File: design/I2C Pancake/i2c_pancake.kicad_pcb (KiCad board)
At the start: 4 copper layers, 74.9 x 45 mm, 41 parts, among them J1 Conn_01x03, J2 Conn_01x03, J3 Conn_01x05_Male, J4 Conn_01x04, J5 Conn_01x04, J6 Conn_01x04, J7 Conn_01x05_Male, J8 Conn_01x05_Female, SW1 SW_DIP_x04, U1 INA826, U2 TL750M10CKVU, U3 INA826, U4 INA826, U6 PIC16F1826-ISO

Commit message: Add test points to the Pancake board.
Test points were added to the outputs of each strain guage amp.
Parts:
- added STR1: TestPoint, custom:TestPoint, F.Cu at (128.1, 107.9)
- added STR2: TestPoint, custom:TestPoint, B.Cu at (135.6, 124.0)
- added STR3: TestPoint, custom:TestPoint, B.Cu at (115.6, 122.6)
- C3: footprint Capacitor_SMD:C_0805_2012Metric_Pad1.15x1.40mm_HandSolder -> footprints:C_0805_HandSoldering
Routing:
- net /STRAIN_OUT_2: track 36.8 -> 40.6 mm
- net /STRAIN_OUT_1: track 34.9 -> 37.9 mm
- net /STRAIN_OUT_3: track 24.4 -> 27.2 mm
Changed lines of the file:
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@@
     (thickness 1.6)
     (drawings 40)
-    (tracks 466)
+    (tracks 479)
     (zones 0)
-    (modules 41)
+    (modules 44)
     (nets 38)
   )
@@
     (mod_text_size 1 1)
     (mod_text_width 0.15)
-    (pad_size 6.7564 6.9342)
-    (pad_drill 0)
+    (pad_size 1.524 1.524)
+    (pad_drill 0.762)
     (pad_to_mask_clearance 0)
     (aux_axis_origin 0 0)
@@
     (add_net /SDA)
   )
+  (module custom:TestPoint (layer B.Cu)
+    (at 135.6026 124.0168)
+    (fp_text reference STR2 (at 0 -0.5) (layer B.SilkS)
+      (effects (font (size 1 1) (thickness 0.15)) (justify mirror))
+    )
+    (fp_text value TestPoint (at 0 0.5) (layer B.Fab)
+      (effects (font (size 1 1) (thickness 0.15)) (justify mirror))
+    )
+    (fp_circle (center 0 -3) (end 1 -3) (layer B.SilkS) (width 0.12))
+    (pad 1 thru_hole circle (at 0 -3) (size 1.524 1.524) (drill 0.762) (layers *.Cu *.Mask)
+      (net 6 /STRAIN_OUT_2))
+  )
+  (module custom:TestPoint (layer F.Cu)
+    (at 128.135 107.9386)
+    (fp_text reference STR1 (at 0 0.5) (layer F.SilkS)
+      (effects (font (size 1 1) (thickness 0.15)))
+    )
+    (fp_text value TestPoint (at 0 -0.5) (layer F.Fab)
+      (effects (font (size 1 1) (thickness 0.15)))
+    )
+    (fp_circle (center 0 3) (end 1 3) (layer F.SilkS) (width 0.12))
+    (pad 1 thru_hole circle (at 0 3) (size 1.524 1.524) (drill 0.762) (layers *.Cu *.Mask)
+      (net 7 /STRAIN_OUT_1))
+  )
+  (module footprints:C_0805_HandSoldering (layer B.Cu)
+    (at 149.09 107.8424 270)
+    (descr "Capacitor SMD 0805, hand soldering")
+    (tags "capacitor 0805")
+    (attr smd)
+    (fp_text reference C3 (at 3.302 0 90) (layer B.SilkS)
+      (effects (font (size 1 1) (thickness 0.15)) (justify mirror))
+    )
+    (fp_text value "10 uF" (at 0 -1.75 90) (layer B.Fab)
+      (effects (font (size 1 1) (thickness 0.15)) (justify mirror))
+    )
+    (fp_line (start 2.25 -0.87) (end -2.25 -0.87) (layer B.CrtYd) (width 0.05))
+    (fp_line (start 2.25 -0.87) (end 2.25 0.88) (layer B.CrtYd) (width 0.05))
+    (fp_line (start -2.25 0.88) (end -2.25 -0.87) (layer B.CrtYd) (width 0.05))
+    (fp_line (start -2.25 0.88) (end 2.25 0.88) (layer B.CrtYd) (width 0.05))
+    (fp_line (start -0.5 -0.85) (end 0.5 -0.85) (layer B.SilkS) (width 0.12))
+    (fp_line (start 0.5 0.85) (end -0.5 0.85) (layer B.SilkS) (width 0.12))
+    (fp_line (start -1 0.62) (end 1 0.62) (layer B.Fab) (width 0.1))
+    (fp_line (start 1 0.62) (end 1 -0.62) (layer B.Fab) (width 0.1))
+    (fp_line (start 1 -0.62) (end -1 -0.62) (layer B.Fab) (width 0.1))
+    (fp_line (start -1 -0.62) (end -1 0.62) (layer B.Fab) (width 0.1))
+    (fp_text user %R (at 0 1.75 90) (layer B.Fab)
+      (effects (font (size 1 1) (thickness 0.15)) (justify mirror))
+    )
+    (pad 2 smd rect (at 1.25 0 270) (size 1.5 1.25) (layers B.Cu B.Paste B.Mask)
+      (net 1 GND))
+    (pad 1 smd rect (at -1.25 0 270) (size 1.5 1.25) (layers B.Cu B.Paste B.Mask)
+      (net 2 +10V))
+    (model Capacitors_SMD.3dshapes/C_0805.wrl
+      (at (xyz 0 0 0))
+      (scale (xyz 1 1 1))
+      (rotate (xyz 0 0 0))
+    )
+  )
+  (module custom:TestPoint (layer B.Cu)
+    (at 115.6382 122.6198)
+    (fp_text reference STR3 (at 3.4798 -2.1844) (layer B.SilkS)
+      (effects (font (size 1 1) (thickness 0.15)) (justify mirror))
+    )
+    (fp_text value TestPoint (at 3.7846 -1.5748) (layer B.Fab)
+      (effects (font (size 1 1) (thickness 0.15)) (justify mirror))
+    )
+    (fp_circle (center 0 -3) (end 1 -3) (layer B.SilkS) (width 0.12))
+    (pad 1 thru_hole circle (at 0 -3) (size 1.524 1.524) (drill 0.762) (layers *.Cu *.Mask)
+      (net 5 /STRAIN_OUT_3))
+  )
   (module Fuse:Fuse_0805_2012Metric_Pad1.15x1.40mm_HandSolder (layer F.Cu)
     (at 142.994 113.2218 270)
@@
       (net 20 "Net-(C1-Pad1)"))
     (model ${KISYS3DMOD}/Fuse.3dshapes/Fuse_0805_2012Metric.wrl
-      (at (xyz 0 0 0))
-      (scale (xyz 1 1 1))
-      (rotate (xyz 0 0 0))
-    )
-  )
-  (module Capacitor_SMD:C_0805_2012Metric_Pad1.15x1.40mm_HandSolder (layer B.Cu)
-    (at 149.09 107.8424 270)
-    (descr "Capacitor SMD 0805 (2012 Metric), square (rectangular) end terminal, IPC_7351 nominal with elongated pad for handsoldering. (Body size source: https://docs.google.com/spreadsheets/d/1BsfQQcO9C6DZCsRaXUlFlo91Tg2WpOkGARC1WS5S8t0/edit?usp=sharing), generated with kicad-footprint-generator")
-    (tags "capacitor handsolder")
-    (attr smd)
-    (fp_text reference C3 (at 0 1.65 90) (layer B.SilkS)
-      (effects (font (size 1 1) (thickness 0.15)) (justify mirror))
-    )
-    (fp_text value "10 uF" (at 0 -1.65 90) (layer B.Fab)
-      (effects (font (size 1 1) (thickness 0.15)) (justify mirror))
-    )
-    (fp_text user %R (at 0 0 90) (layer B.Fab)
-      (effects (font (size 0.5 0.5) (thickness 0.08)) (justify mirror))
-    )
-    (fp_line (start 1.85 -0.95) (end -1.85 -0.95) (layer B.CrtYd) (width 0.05))
-    (fp_line (start 1.85 0.95) (end 1.85 -0.95) (layer B.CrtYd) (width 0.05))
-    (fp_line (start -1.85 0.95) (end 1.85 0.95) (layer B.CrtYd) (width 0.05))
-    (fp_line (start -1.85 -0.95) (end -1.85 0.95) (layer B.CrtYd) (width 0.05))
-    (fp_line (start -0.261252 -0.71) (end 0.261252 -0.71) (layer B.SilkS) (width 0.12))
-    (fp_line (start -0.261252 0.71) (end 0.261252 0.71) (layer B.SilkS) (width 0.12))
-    (fp_line (start 1 -0.6) (end -1 -0.6) (layer B.Fab) (width 0.1))
-    (fp_line (start 1 0.6) (end 1 -0.6) (layer B.Fab) (width 0.1))
-    (fp_line (start -1 0.6) (end 1 0.6) (layer B.Fab) (width 0.1))
-    (fp_line (start -1 -0.6) (end -1 0.6) (layer B.Fab) (width 0.1))
-    (pad 2 smd roundrect (at 1.025 0 270) (size 1.15 1.4) (layers B.Cu B.Paste B.Mask) (roundrect_rratio 0.217391)
-      (net 1 GND))
-    (pad 1 smd roundrect (at -1.025 0 270) (size 1.15 1.4) (layers B.Cu B.Paste B.Mask) (roundrect_rratio 0.217391)
-      (net 2 +10V))
-    (model ${KISYS3DMOD}/Capacitor_SMD.3dshapes/C_0805_2012Metric.wrl
       (at (xyz 0 0 0))
       (scale (xyz 1 1 1))
@@
   (segment (start 114.888481 116.147399) (end 110.008609 116.147399) (width 0.2032) (layer B.Cu) (net 5))
   (segment (start 110.008609 116.147399) (end 106.49419 119.661818) (width 0.2032) (layer B.Cu) (net 5))
-  (segment (start 117.398482 118.6574) (end 114.888481 116.147399) (width 0.2032) (layer B.Cu) (net 5))
   (segment (start 121.8856 118.6574) (end 117.398482 118.6574) (width 0.2032) (layer B.Cu) (net 5))
+  (segment (start 115.565841 116.824759) (end 114.888481 116.147399) (width 0.2032) (layer B.Cu) (net 5))
+  (segment (start 115.642041 118.538329) (end 115.642041 116.900959) (width 0.2032) (layer B.Cu) (net 5))
+  (segment (start 115.6382 118.54217) (end 115.642041 118.538329) (width 0.2032) (layer B.Cu) (net 5))
+  (segment (start 115.6382 119.6198) (end 115.6382 118.54217) (width 0.2032) (layer B.Cu) (net 5))
+  (segment (start 117.398482 118.6574) (end 115.642041 116.900959) (width 0.2032) (layer B.Cu) (net 5))
+  (segment (start 115.642041 116.900959) (end 115.565841 116.824759) (width 0.2032) (layer B.Cu) (net 5))
   (segment (start 118.638497 112.580179) (end 126.265118 120.2068) (width 0.2032) (layer F.Cu) (net 6))
   (segment (start 109.097179 112.580179) (end 118.638497 112.580179) (width 0.2032) (layer F.Cu) (net 6))
   (segment (start 106.5704 108.3502) (end 106.5704 110.0534) (width 0.2032) (layer F.Cu) (net 6))
   (segment (start 106.5704 110.0534) (end 109.097179 112.580179) (width 0.2032) (layer F.Cu) (net 6))
-  (segment (start 126.265118 120.2068) (end 133.215 120.2068) (width 0.2032) (layer F.Cu) (net 6))
   (via (at 133.723 119.6988) (size 0.762) (drill 0.4191) (layers F.Cu B.Cu) (net 6))
   (segment (start 133.215 120.2068) (end 133.723 119.6988) (width 0.2032) (layer F.Cu) (net 6))
@@
   (segment (start 133.2658 118.6574) (end 131.2856 118.6574) (width 0.2032) (layer B.Cu) (net 6))
   (segment (start 133.723 119.1146) (end 133.2658 118.6574) (width 0.2032) (layer B.Cu) (net 6))
+  (segment (start 134.52497 121.0168) (end 134.52217 121.0196) (width 0.2032) (layer F.Cu) (net 6))
+  (segment (start 135.6026 121.0168) (end 134.52497 121.0168) (width 0.2032) (layer F.Cu) (net 6))
+  (segment (start 132.9356 121.0196) (end 132.1228 120.2068) (width 0.2032) (layer F.Cu) (net 6))
+  (segment (start 134.52217 121.0196) (end 132.9356 121.0196) (width 0.2032) (layer F.Cu) (net 6))
+  (segment (start 126.265118 120.2068) (end 132.1228 120.2068) (width 0.2032) (layer F.Cu) (net 6))
+  (segment (start 132.1228 120.2068) (end 133.215 120.2068) (width 0.2032) (layer F.Cu) (net 6))
   (segment (start 108.198399 102.943601) (end 108.198399 108.347399) (width 0.2032) (layer B.Cu) (net 7))
   (segment (start 110.054 102.288) (end 108.854 102.288) (width 0.2032) (layer B.Cu) (net 7))
@@
   (via (at 129.2526 115.076) (size 0.762) (drill 0.4191) (layers F.Cu B.Cu) (net 7))
   (segment (start 119.5498 112.0534) (end 126.23 112.0534) (width 0.2032) (layer F.Cu) (net 7))
-  (segment (start 126.23 112.0534) (end 129.2526 115.076) (width 0.2032) (layer F.Cu) (net 7))
   (segment (start 130.5856 117.3874) (end 131.2856 117.3874) (width 0.2032) (layer B.Cu) (net 7))
   (segment (start 129.2526 116.0544) (end 130.5856 117.3874) (width 0.2032) (layer B.Cu) (net 7))
   (segment (start 129.2526 115.076) (end 129.2526 116.0544) (width 0.2032) (layer B.Cu) (net 7))
+  (segment (start 128.135 113.9076) (end 128.1096 113.933) (width 0.2032) (layer F.Cu) (net 7))
+  (segment (start 128.135 110.9386) (end 128.135 113.9076) (width 0.2032) (layer F.Cu) (net 7))
+  (segment (start 126.23 112.0534) (end 128.1096 113.933) (width 0.2032) (layer F.Cu) (net 7))
+  (segment (start 128.1096 113.933) (end 129.2526 115.076) (width 0.2032) (layer F.Cu) (net 7))
   (segment (start 104.254 103.558) (end 103.054 103.558) (width 0.2032) (layer B.Cu) (net 8))
   (segment (start 104.909601 102.902399) (end 104.254 103.558) (width 0.2032) (layer B.Cu) (net 8))

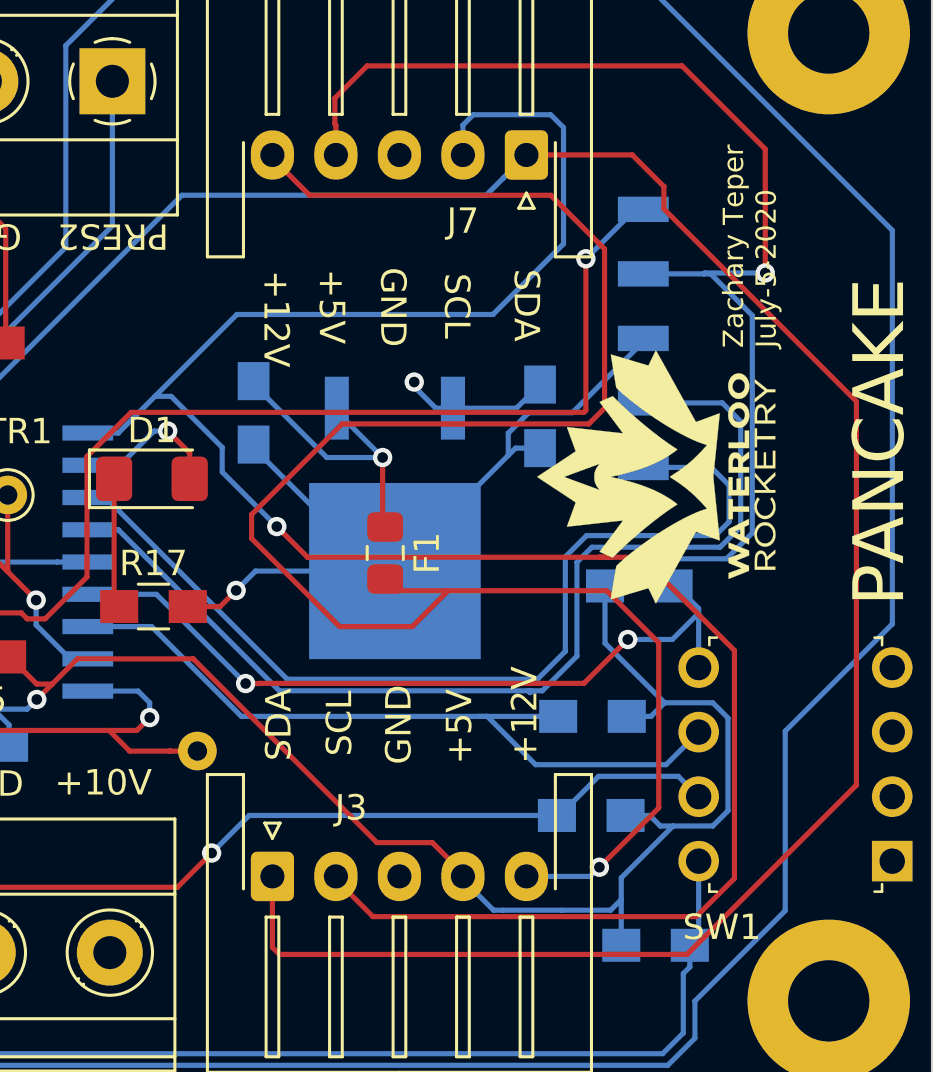
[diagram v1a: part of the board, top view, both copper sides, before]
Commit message: Improve SCL track spacing.
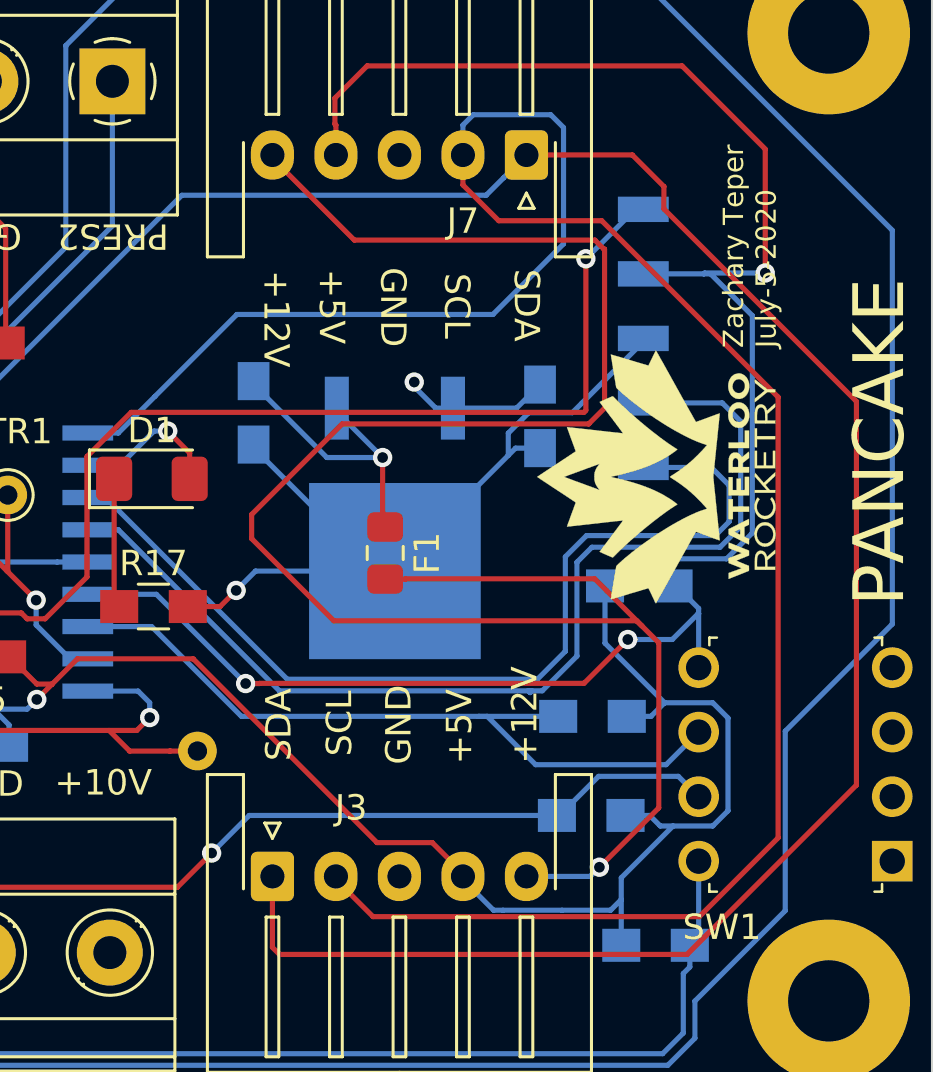
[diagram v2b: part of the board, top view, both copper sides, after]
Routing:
- net +12V: track 71.7 -> 79.0 mm
- net /SCL: track 85.9 -> 85.7 mm, vias 1 -> 0
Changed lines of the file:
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@@
     (thickness 1.6)
     (drawings 40)
-    (tracks 479)
+    (tracks 476)
     (zones 0)
     (modules 44)
@@
     (visible_elements 7FFFFFFF)
     (pcbplotparams
-      (layerselection 0x010f0_80000001)
+      (layerselection 0x010ff_ffffffff)
       (usegerberextensions true)
       (usegerberattributes false)
@@
       (drillshape 0)
       (scaleselection 1)
-      (outputdirectory "../../fab/strain_gauges_rtr/"))
+      (outputdirectory "C:/Users/zacha/Desktop/Zachary/Rocketry/daq/"))
   )
   (net 0 "")
@@
   (segment (start 153.7636 123.2548) (end 151.4268 125.5916) (width 0.2032) (layer F.Cu) (net 24))
   (segment (start 153.7636 116.756318) (end 153.7636 123.2548) (width 0.2032) (layer F.Cu) (net 24))
-  (segment (start 151.716582 114.7093) (end 153.7636 116.756318) (width 0.2032) (layer F.Cu) (net 24))
-  (segment (start 145.4181 114.7093) (end 151.716582 114.7093) (width 0.2032) (layer F.Cu) (net 24))
-  (segment (start 142.994 114.7093) (end 145.4181 114.7093) (width 0.2032) (layer F.Cu) (net 24))
+  (segment (start 151.716582 114.7093) (end 153.101241 116.093959) (width 0.2032) (layer F.Cu) (net 24))
+  (segment (start 153.101241 116.093959) (end 153.7636 116.756318) (width 0.2032) (layer F.Cu) (net 24))
+  (segment (start 143.794 114.2468) (end 143.803 114.2378) (width 0.2032) (layer F.Cu) (net 24))
+  (segment (start 142.994 114.2468) (end 143.794 114.2468) (width 0.2032) (layer F.Cu) (net 24))
+  (segment (start 151.245082 114.2378) (end 151.716582 114.7093) (width 0.2032) (layer F.Cu) (net 24))
+  (segment (start 143.803 114.2378) (end 151.245082 114.2378) (width 0.2032) (layer F.Cu) (net 24))
+  (segment (start 141.778799 100.902799) (end 138.554 97.678) (width 0.2032) (layer F.Cu) (net 24))
+  (segment (start 151.246969 100.902799) (end 141.778799 100.902799) (width 0.2032) (layer F.Cu) (net 24))
+  (segment (start 151.630001 101.257547) (end 151.601717 101.257547) (width 0.2032) (layer F.Cu) (net 24))
+  (segment (start 151.630001 107.518389) (end 151.630001 101.257547) (width 0.2032) (layer F.Cu) (net 24))
   (segment (start 138.554 97.678) (end 138.554 97.553) (width 0.2032) (layer F.Cu) (net 24))
-  (segment (start 140.01361 99.13761) (end 138.554 97.678) (width 0.2032) (layer F.Cu) (net 24))
-  (segment (start 149.510064 99.13761) (end 140.01361 99.13761) (width 0.2032) (layer F.Cu) (net 24))
-  (segment (start 151.630001 107.518389) (end 151.630001 101.257547) (width 0.2032) (layer F.Cu) (net 24))
+  (segment (start 153.101241 116.093959) (end 152.897025 115.889743) (width 0.2032) (layer F.Cu) (net 24))
+  (segment (start 151.601717 101.257547) (end 151.246969 100.902799) (width 0.2032) (layer F.Cu) (net 24))
   (segment (start 151.006582 108.141808) (end 151.630001 107.518389) (width 0.2032) (layer F.Cu) (net 24))
-  (segment (start 141.299301 108.141809) (end 151.006582 108.141808) (width 0.2032) (layer F.Cu) (net 24))
-  (segment (start 145.4181 114.7601) (end 144.0608 116.1174) (width 0.2032) (layer F.Cu) (net 24))
-  (segment (start 151.630001 101.257547) (end 149.510064 99.13761) (width 0.2032) (layer F.Cu) (net 24))
-  (segment (start 145.4181 114.7093) (end 145.4181 114.7601) (width 0.2032) (layer F.Cu) (net 24))
-  (segment (start 144.0608 116.1174) (end 141.19771 116.1174) (width 0.2032) (layer F.Cu) (net 24))
-  (segment (start 141.19771 116.1174) (end 137.736199 112.655889) (width 0.2032) (layer F.Cu) (net 24))
+  (segment (start 152.897025 115.889743) (end 140.970053 115.889743) (width 0.2032) (layer F.Cu) (net 24))
+  (segment (start 140.970053 115.889743) (end 137.736199 112.655889) (width 0.2032) (layer F.Cu) (net 24))
   (segment (start 137.736199 112.655889) (end 137.736199 111.704911) (width 0.2032) (layer F.Cu) (net 24))
   (segment (start 137.736199 111.704911) (end 141.299301 108.141809) (width 0.2032) (layer F.Cu) (net 24))
+  (segment (start 141.299301 108.141809) (end 151.006582 108.141808) (width 0.2032) (layer F.Cu) (net 24))
   (segment (start 150.01361 101.0531) (end 147.2358 103.83091) (width 0.2032) (layer B.Cu) (net 25))
   (segment (start 150.01361 96.471936) (end 150.01361 101.0531) (width 0.2032) (layer B.Cu) (net 25))
@@
   (segment (start 132.4888 108.4974) (end 131.2856 108.4974) (width 0.2032) (layer B.Cu) (net 25))
   (segment (start 147.2358 103.83091) (end 137.15529 103.83091) (width 0.2032) (layer B.Cu) (net 25))
-  (segment (start 133.9314 107.0548) (end 134.5664 107.0548) (width 0.2032) (layer B.Cu) (net 25))
   (segment (start 133.9314 107.0548) (end 132.4888 108.4974) (width 0.2032) (layer B.Cu) (net 25))
   (segment (start 137.15529 103.83091) (end 133.9314 107.0548) (width 0.2032) (layer B.Cu) (net 25))
-  (via (at 138.7268 112.1804) (size 0.762) (drill 0.4191) (layers F.Cu B.Cu) (net 25))
-  (segment (start 136.577799 110.031399) (end 138.7268 112.1804) (width 0.2032) (layer B.Cu) (net 25))
-  (segment (start 134.5664 107.0548) (end 136.577799 109.066199) (width 0.2032) (layer B.Cu) (net 25))
-  (segment (start 136.577799 109.066199) (end 136.577799 110.031399) (width 0.2032) (layer B.Cu) (net 25))
   (segment (start 141.054 126.078) (end 141.054 125.953) (width 0.2032) (layer F.Cu) (net 25))
   (segment (start 142.51361 127.53761) (end 141.054 126.078) (width 0.2032) (layer F.Cu) (net 25))
-  (segment (start 155.2356 127.53761) (end 142.51361 127.53761) (width 0.2032) (layer F.Cu) (net 25))
-  (segment (start 156.743601 126.029609) (end 155.2356 127.53761) (width 0.2032) (layer F.Cu) (net 25))
-  (segment (start 138.7268 112.1804) (end 139.93359 113.38719) (width 0.2032) (layer F.Cu) (net 25))
-  (segment (start 153.0744 113.38719) (end 151.41439 113.38719) (width 0.2032) (layer F.Cu) (net 25))
-  (segment (start 156.743601 117.056391) (end 153.0744 113.38719) (width 0.2032) (layer F.Cu) (net 25))
-  (segment (start 156.743601 126.029609) (end 156.743601 117.056391) (width 0.2032) (layer F.Cu) (net 25))
-  (segment (start 139.93359 113.38719) (end 151.41439 113.38719) (width 0.2032) (layer F.Cu) (net 25))
-  (segment (start 151.41439 113.38719) (end 151.906608 113.38719) (width 0.2032) (layer F.Cu) (net 25))
+  (segment (start 155.358388 127.53761) (end 142.51361 127.53761) (width 0.2032) (layer F.Cu) (net 25))
+  (segment (start 158.4626 124.433398) (end 155.358388 127.53761) (width 0.2032) (layer F.Cu) (net 25))
+  (segment (start 158.4626 107.084344) (end 158.4626 124.433398) (width 0.2032) (layer F.Cu) (net 25))
+  (segment (start 151.519056 100.1408) (end 158.4626 107.084344) (width 0.2032) (layer F.Cu) (net 25))
+  (segment (start 147.4636 100.1408) (end 151.519056 100.1408) (width 0.2032) (layer F.Cu) (net 25))
+  (segment (start 146.054 98.7312) (end 147.4636 100.1408) (width 0.2032) (layer F.Cu) (net 25))
+  (segment (start 146.054 97.553) (end 146.054 98.7312) (width 0.2032) (layer F.Cu) (net 25))
   (segment (start 147.655628 98.451372) (end 148.554 97.553) (width 0.2032) (layer B.Cu) (net 26))
   (segment (start 146.96939 99.13761) (end 147.655628 98.451372) (width 0.2032) (layer B.Cu) (net 26))
